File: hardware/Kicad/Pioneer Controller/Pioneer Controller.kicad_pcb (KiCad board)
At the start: 2 copper layers, 72 x 96 mm, 36 parts, among them J1 Sensor Connector, J2 Power (USBC), J3 Arduino-NANO-33, J4 Conn_Coaxial, SW1 SW_MEC_5E, SW2 SW_MEC_5E, SW3 SW_MEC_5E, SW4 SW_MEC_5E, U1 ESP32-S3, U2 2821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

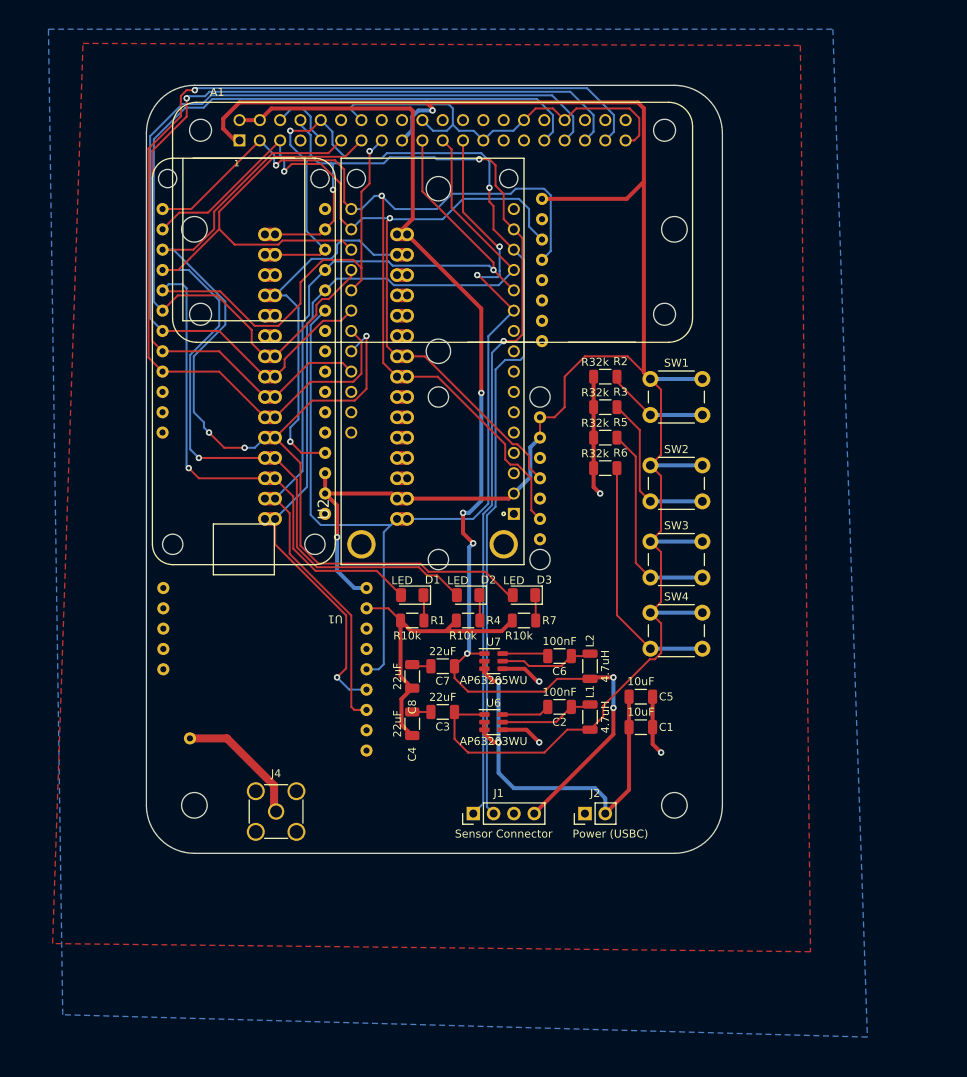
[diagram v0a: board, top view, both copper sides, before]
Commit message: PCB 3D model
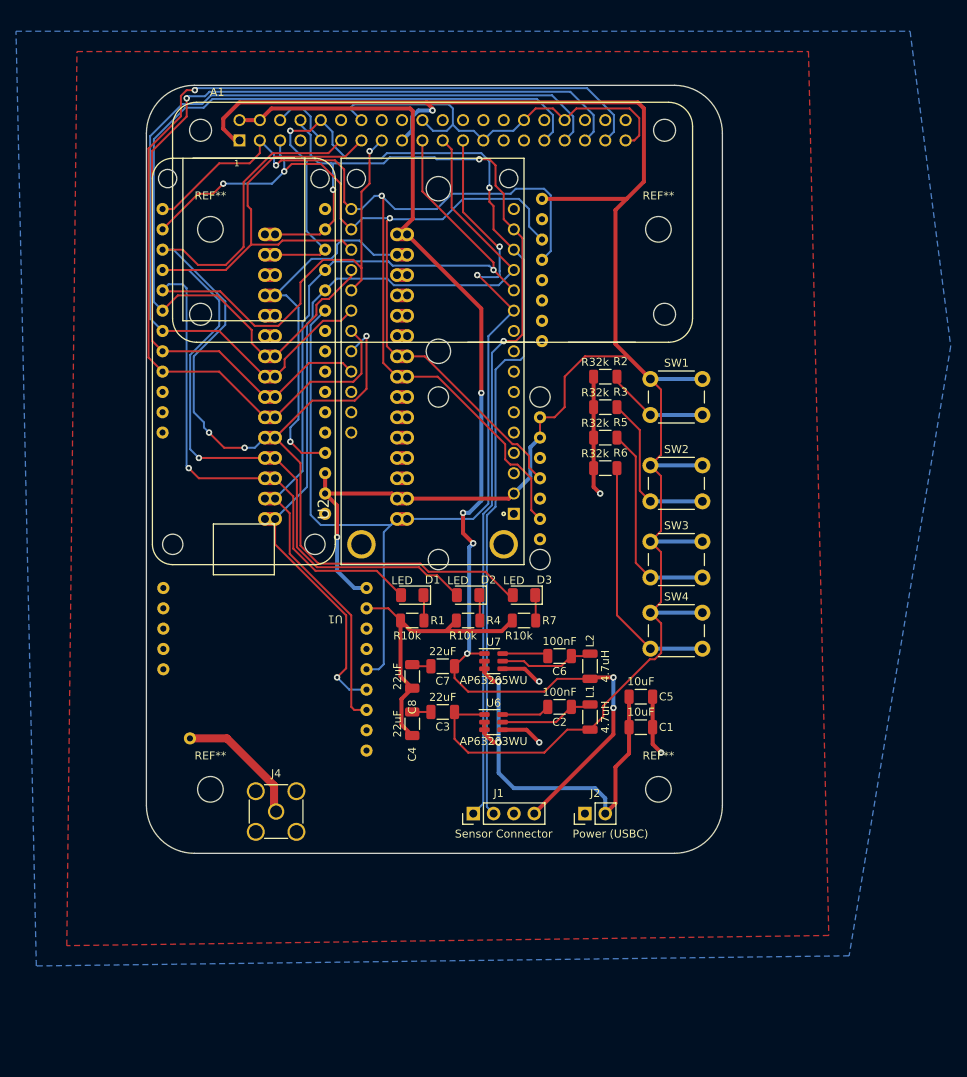
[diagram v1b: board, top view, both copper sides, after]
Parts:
- added REF**: MountingHole_3.2mm_M3, MountingHole:MountingHole_3.2mm_M3, F.Cu at (37.0, 40.0)
- added REF**: MountingHole_3.2mm_M3, MountingHole:MountingHole_3.2mm_M3, F.Cu at (93.0, 110.0)
- added REF**: MountingHole_3.2mm_M3, MountingHole:MountingHole_3.2mm_M3, F.Cu at (37.0, 110.0)
- added REF**: MountingHole_3.2mm_M3, MountingHole:MountingHole_3.2mm_M3, F.Cu at (93.0, 40.0)
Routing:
- net /LED3: track 134.1 -> 139.1 mm
- net /SCL: track 108.7 -> 107.6 mm, vias 2 -> 3
- net /LED2: track 124.2 -> 123.2 mm
- net /SDA: track 121.2 -> 122.2 mm
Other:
- outline, holes or cut-outs redrawn

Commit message: stuff
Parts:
- added SW5: SW_DIP_x02, Button_Switch_THT:SW_DIP_SPSTx02_Slide_9.78x7.26mm_W7.62mm_P2.54mm, F.Cu at (86.4, 78.7)
- L1, L2: value 4.7uH -> INDUCTOR 4.7uH
- moved SW1 2.54 mm to (92.0, 61.2)
- moved SW2 0.64 mm to (92.0, 70.1)
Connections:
- A1 pad 38: unconnected-(A1-Pad38) -> /SW6
- A1 pad 40: unconnected-(A1-Pad40) -> /SW5
- J3 pad 6: unconnected-(J3-Pad6) -> /SW5
- J3 pad 7: unconnected-(J3-Pad7) -> /SW6
- U1 pad A4: unconnected-(U1-PadA4) -> /SW5
- U1 pad A5: unconnected-(U1-PadA5) -> /SW6
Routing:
- net /SW6: track 0.00 -> 108.4 mm, vias 0 -> 2
- net /SW5: track 0.00 -> 107.8 mm, vias 0 -> 2
- net +3V3: track 289.6 -> 296.1 mm
- net Net-(R2-Pad1): track 13.0 -> 15.6 mm
- net Net-(R3-Pad1): track 20.0 -> 21.1 mm
- net Net-(R5-Pad1): track 25.7 -> 26.4 mm

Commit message: more PCb updates
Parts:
- J2: value Power (USBC) -> Power
- moved J4 5.79 mm to (51.0, 112.8)
- moved REF** 3.00 mm to (93.0, 113.0)
- moved REF** 3.00 mm to (37.0, 113.0)
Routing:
- net /SMA: track 16.3 -> 20.3 mm
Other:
- board size 72 x 96 mm -> 72 x 98.8 mm
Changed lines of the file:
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@@
   )
   (footprint "Connector_Coaxial:SMA_Amphenol_132134-11_Vertical" (layer "F.Cu")
-    (at 45.212 112.776)
+    (at 51 112.776)
     (descr "https://www.amphenolrf.com/downloads/dl/file/id/3406/product/2975/132134_11_customer_drawing.pdf")
     (tags "SMA THT Female Jack Vertical ExtendedLegs")
@@
       (effects (font (size 1 1) (thickness 0.15)))
     )
-    (fp_text value "Power (USBC)" (at -2.54 3.18 180) (layer "F.SilkS")
+    (fp_text value "Power" (at -2.97 1.18 180) (layer "F.SilkS")
       (effects (font (size 1 1) (thickness 0.15)))
     )
@@
     )
   )
-  (footprint "MountingHole:MountingHole_3.2mm_M3" locked (layer "F.Cu")
-    (at 93 110)
+  (footprint "MountingHole:MountingHole_3.2mm_M3" (layer "F.Cu")
+    (at 93 113)
     (descr "Mounting Hole 3.2mm, no annular, M3")
     (tags "mounting hole 3.2mm no annular m3")
@@
     )
   )
-  (footprint "MountingHole:MountingHole_3.2mm_M3" locked (layer "F.Cu")
-    (at 37 110)
+  (footprint "MountingHole:MountingHole_3.2mm_M3" (layer "F.Cu")
+    (at 37 113)
     (descr "Mounting Hole 3.2mm, no annular, M3")
     (tags "mounting hole 3.2mm no annular m3")
@@
     (fp_circle (center 0 0) (end 3.2 0) (layer "Cmts.User") (width 0.15) (fill none))
     (fp_circle (center 0 0) (end 3.45 0) (layer "F.CrtYd") (width 0.05) (fill none))
-    (pad "" np_thru_hole circle locked (at 0 0) (size 3.2 3.2) (drill 3.2) (layers *.Cu *.Mask))
+    (pad "" np_thru_hole circle (at 0 0) (size 3.2 3.2) (drill 3.2) (layers F&B.Cu *.Mask))
   )
   (footprint "LED_SMD:LED_1206_3216Metric" (layer "F.Cu")
@@
   )
   (gr_arc (start 95 22) (mid 99.242641 23.757359) (end 101 28) (layer "Edge.Cuts") (width 0.1))
-  (gr_line (start 35 118) (end 95 118) (layer "Edge.Cuts") (width 0.1))
-  (gr_line (start 101 112) (end 101 28) (layer "Edge.Cuts") (width 0.1))
-  (gr_arc (start 101 112) (mid 99.242641 116.242641) (end 95 118) (layer "Edge.Cuts") (width 0.1))
+  (gr_line (start 35 120.757359) (end 95 120.757359) (layer "Edge.Cuts") (width 0.1))
+  (gr_line (start 101 114.757359) (end 101 28) (layer "Edge.Cuts") (width 0.1))
+  (gr_arc (start 101 114.757359) (mid 99.242641 119) (end 95 120.757359) (layer "Edge.Cuts") (width 0.1))
   (gr_line (start 35 22) (end 95 22) (layer "Edge.Cuts") (width 0.1))
   (gr_arc (start 29 28) (mid 30.757359 23.757359) (end 35 22) (layer "Edge.Cuts") (width 0.1))
-  (gr_line (start 29 28) (end 29 112) (layer "Edge.Cuts") (width 0.1))
-  (gr_arc (start 35 118) (mid 30.757359 116.242641) (end 29 112) (layer "Edge.Cuts") (width 0.1))
+  (gr_line (start 29 28) (end 29 114.757359) (layer "Edge.Cuts") (width 0.1))
+  (gr_arc (start 35 120.757359) (mid 30.757359 119) (end 29 114.757359) (layer "Edge.Cuts") (width 0.1))
   (segment (start 40.64 24.13) (end 64.008 24.13) (width 0.5) (layer "F.Cu") (net 1))
   (segment (start 51.34 73.025) (end 59.69 73.025) (width 0.5) (layer "F.Cu") (net 1))
@@
   (segment (start 88.9 70.9275) (end 88.9 89.32) (width 0.25) (layer "F.Cu") (net 60))
   (segment (start 92 92.42) (end 98.5 92.42) (width 0.25) (layer "B.Cu") (net 60))
-  (segment (start 39.063227 103.632) (end 44.958 109.526773) (width 1) (layer "F.Cu") (net 77))
+  (segment (start 39.063227 103.632) (end 48.207227 112.776) (width 1) (layer "F.Cu") (net 77))
   (segment (start 34.445 103.632) (end 39.063227 103.632) (width 1) (layer "F.Cu") (net 77))
-  (segment (start 44.958 109.526773) (end 44.958 112.522) (width 1) (layer "F.Cu") (net 77))
-  (segment (start 44.958 112.522) (end 45.212 112.776) (width 1) (layer "F.Cu") (net 77))
+  (segment (start 48.207227 112.776) (end 51 112.776) (width 1) (layer "F.Cu") (net 77))
   (zone (net 5) (net_name "GND") (layer "F.Cu") (hatch edge 0.508)
     (connect_pads (clearance 0.508))

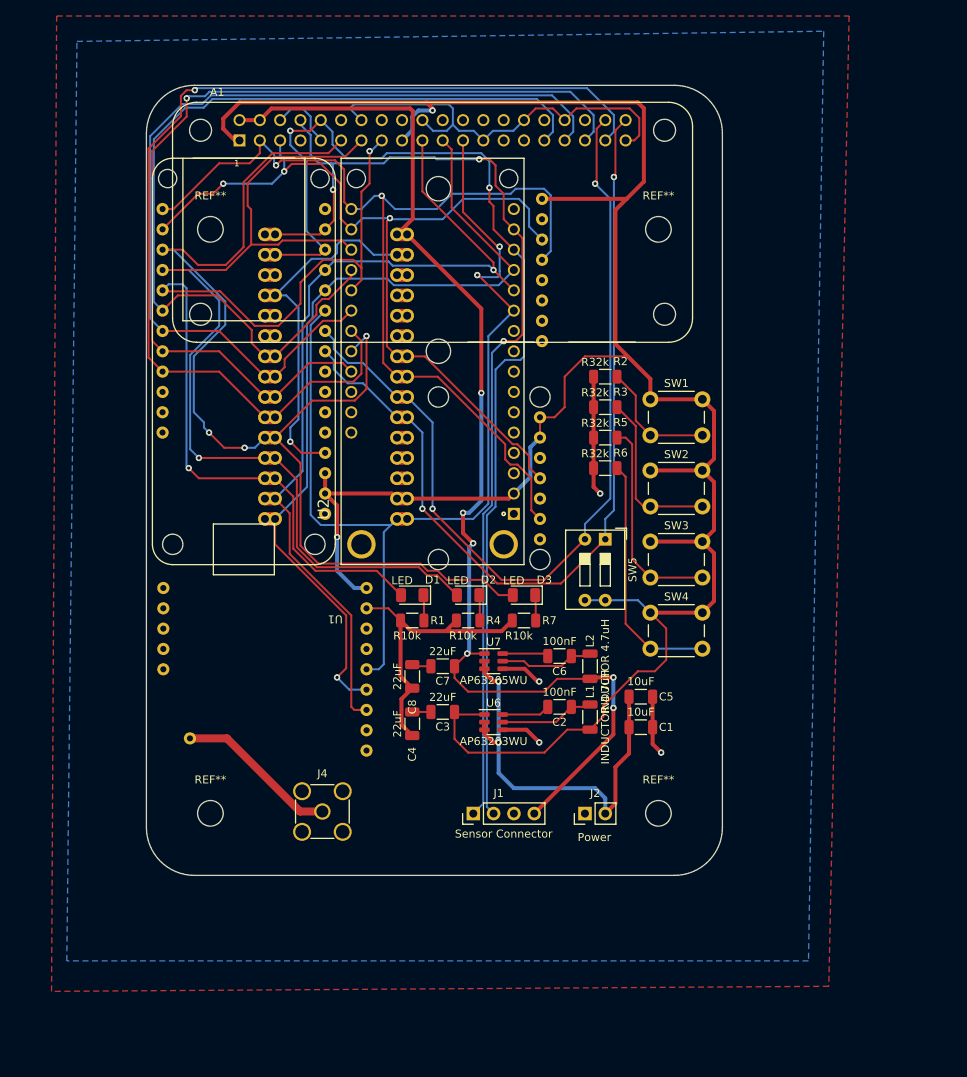
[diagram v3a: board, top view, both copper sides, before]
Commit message: updated 3.3V PMIC
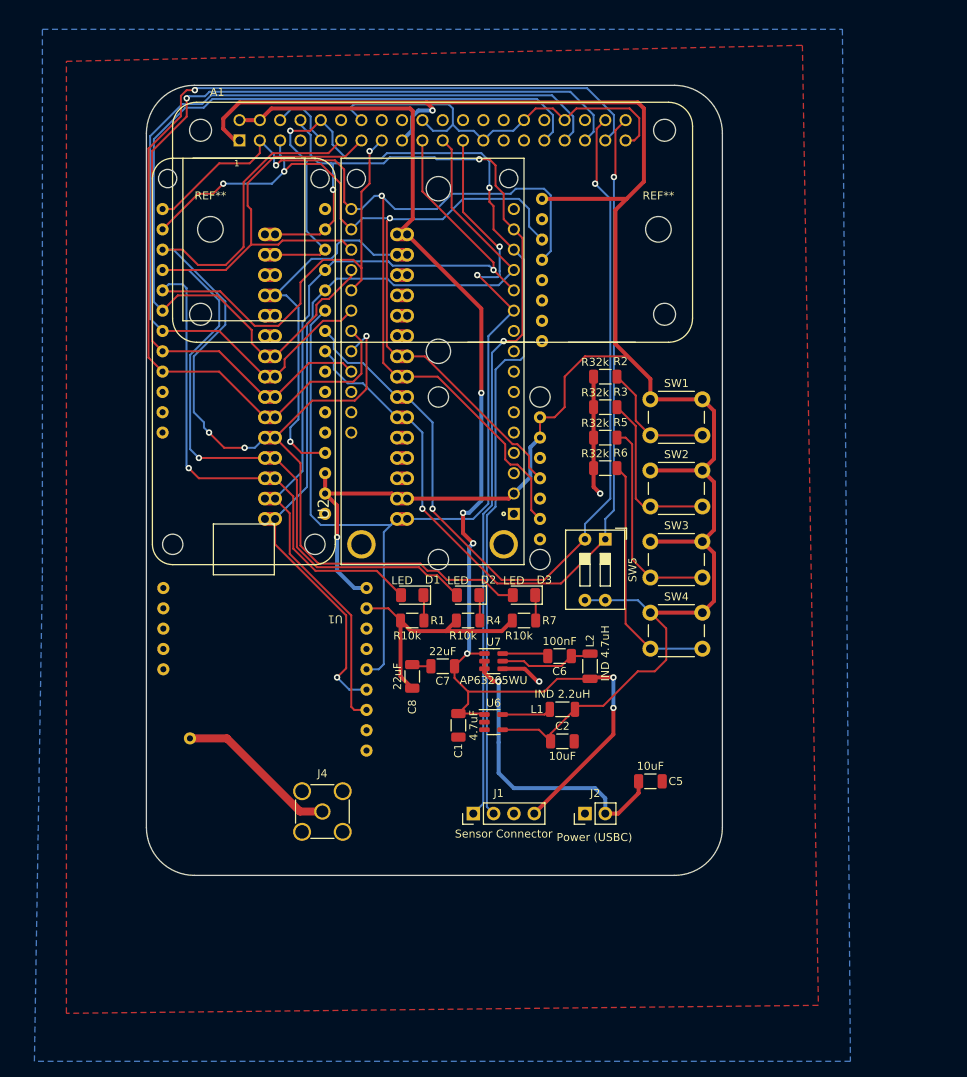
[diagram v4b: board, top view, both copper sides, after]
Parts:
- removed C3, C4: 22uF, Capacitor_SMD:C_1206_3216Metric
- removed the REF** at (93.0, 113.0)
- removed the REF** at (37.0, 113.0)
- C1: value 10uF -> 4.7uF
- C2: value 100nF -> 10uF
- J2: value Power -> Power (USBC)
- L1: value INDUCTOR 4.7uH -> IND 2.2uH
- L2: value INDUCTOR 4.7uH -> IND 4.7uH
- U6: value AP63203WU -> LM3670MF; footprint Package_TO_SOT_SMD:TSOT-23-6 -> Package_TO_SOT_SMD:TSOT-23-5
- moved C1 22.8 mm to (68.0, 102.0), turned to -90 degrees
- moved C5 10.6 mm to (92.0, 109.0)
- moved C2 4.32 mm to (81.0, 104.0), turned to 0 degrees
- moved L1 3.59 mm to (81.0, 100.0), turned to 0 degrees
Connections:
- C1 pad 1: VIN -> +5V
- C2 pad 1: Net-(C2-Pad1) -> +3V3
- C2 pad 2: Net-(C2-Pad2) -> GND
- L1 pad 1: Net-(C2-Pad1) -> Net-(L1-Pad1)
- U6 pad 1: +3V3 -> +5V
- U6 pad 2: VIN -> GND
- U6 pad 3: VIN -> unconnected-(U6-Pad3)
- U6 pad 4: GND -> +3V3
- U6 pad 5: Net-(C2-Pad1) -> Net-(L1-Pad1)
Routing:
- net GND: track 183.8 -> 164.1 mm, vias 5 -> 3
- net +3V3: track 296.1 -> 281.9 mm
- net VIN: track 51.1 -> 38.3 mm, vias 2 -> 1
- net Net-(C2-Pad1): track 11.8 -> 0.00 mm
- net +5V: track 145.4 -> 151.9 mm
- net Net-(L1-Pad1): track 0.00 -> 6.17 mm
- net Net-(C2-Pad2): track 6.04 -> 0.00 mm
- net Net-(C3-Pad2): track 2.34 -> 0.00 mm
